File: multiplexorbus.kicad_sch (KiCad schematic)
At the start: 4 parts

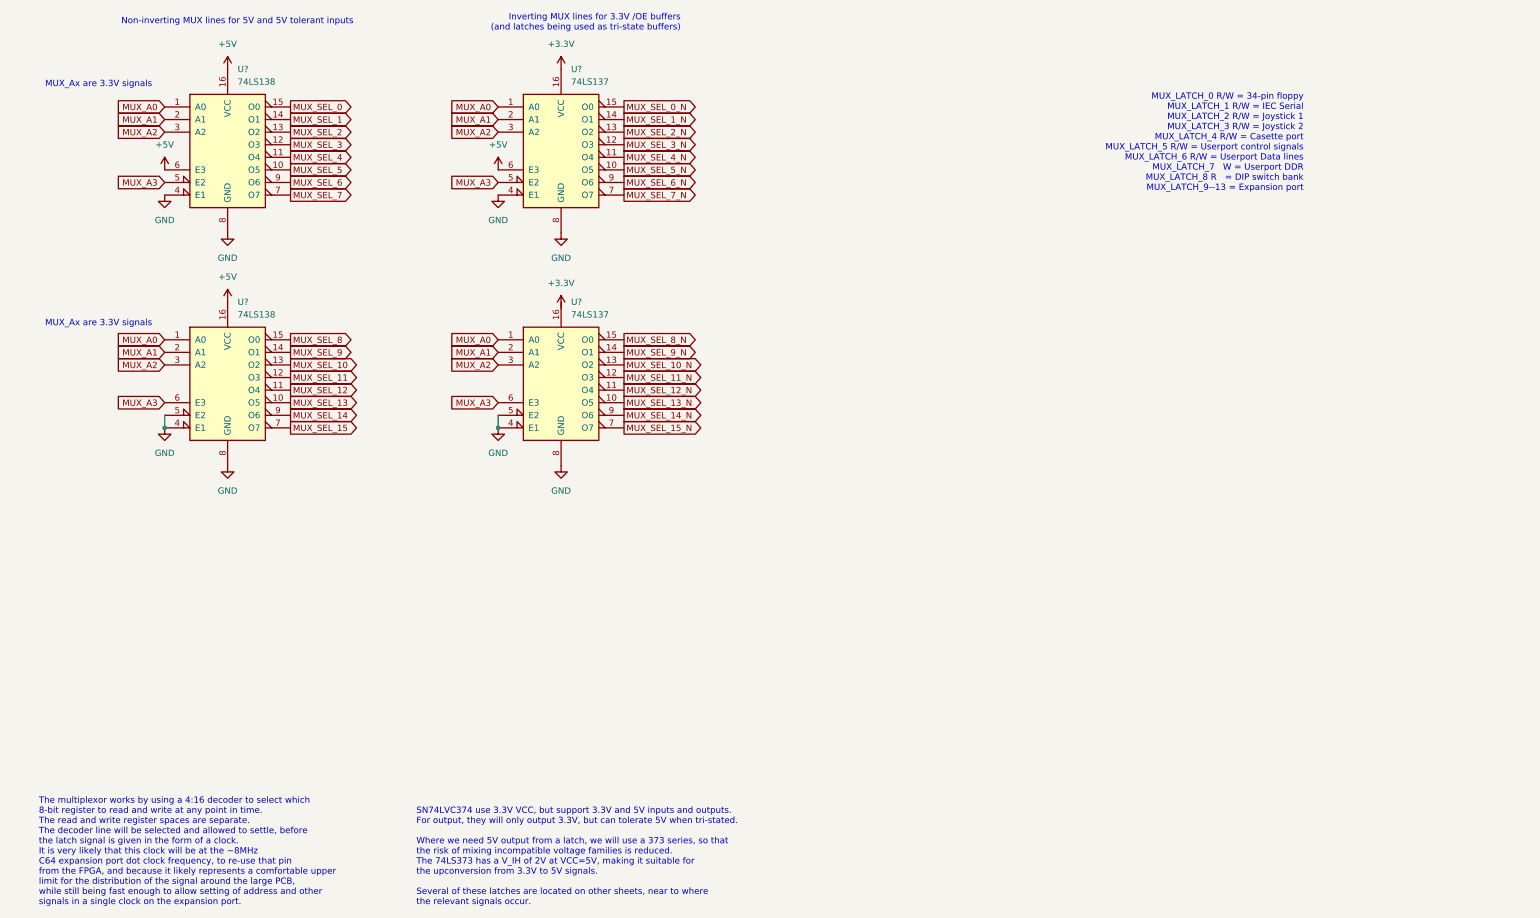
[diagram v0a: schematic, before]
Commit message: beautify the schematics, especially the title-page
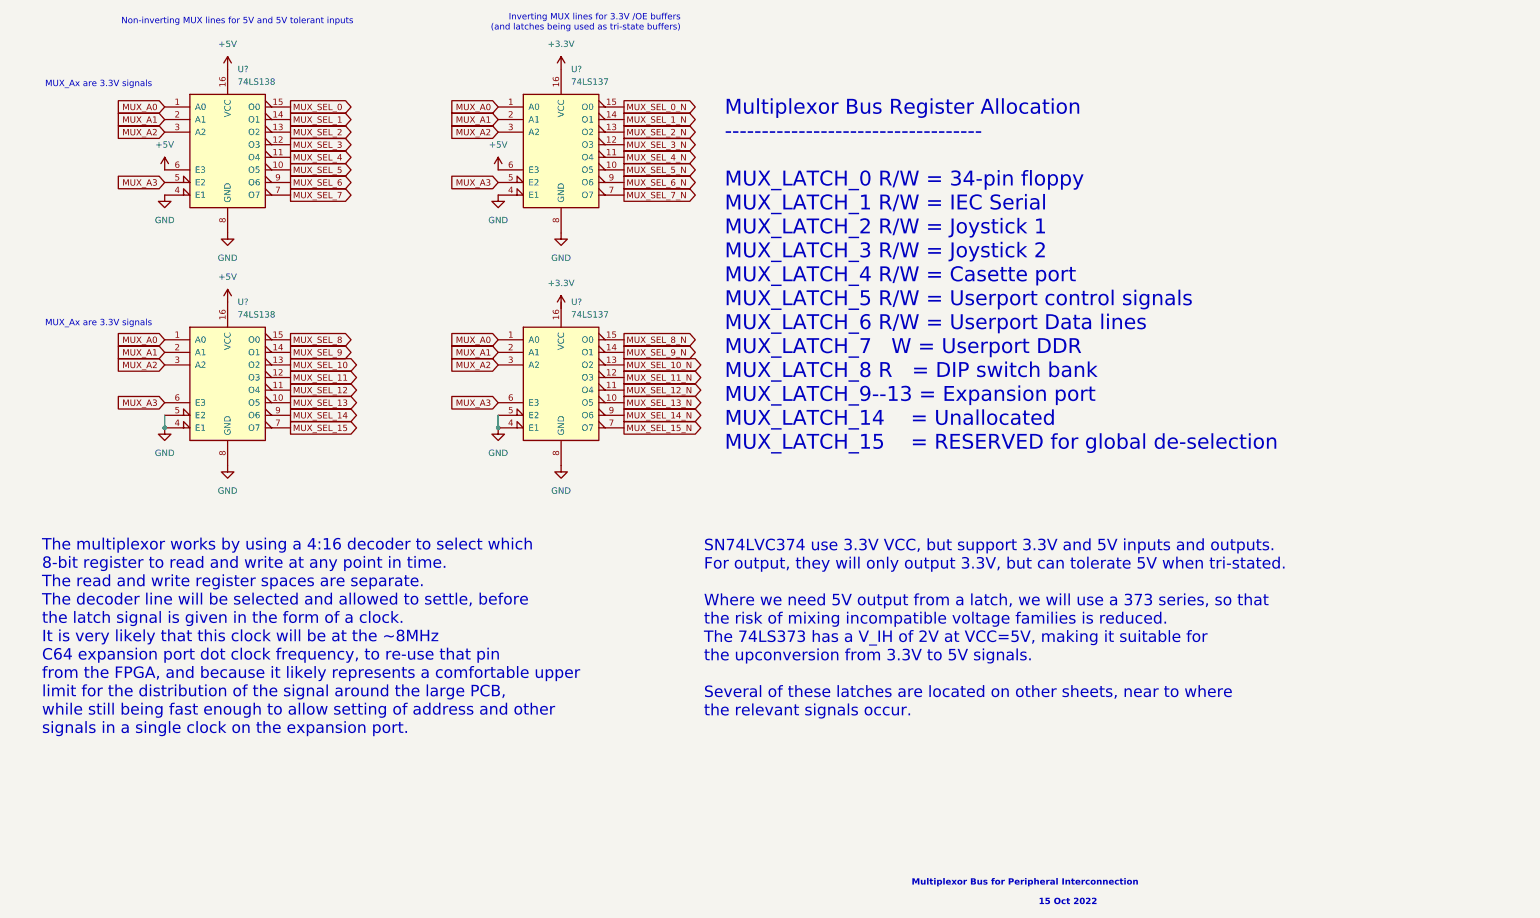
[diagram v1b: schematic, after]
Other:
- note added: "15 Oct 2022"
- note added: "Multiplexor Bus Register Allocation ----------------------------------- MUX_LATCH_0 R/W = 34-pin floppy MUX_LATCH_1 R/W = IEC Serial MUX_LATCH_2 R/W = Joystick 1 MUX_LATCH_3 R/W = Joystick 2 MUX_LATCH_4 R/W = Casette port MUX_LATCH_5 R/W = Userport control signals MUX_LATCH_6 R/W = Userport Data lines MUX_LATCH_7 W = Userport DDR MUX_LATCH_8 R = DIP switch bank MUX_LATCH_9--13 = Expansion port MU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"
- note added: "Multiplexor Bus for Peripheral Interconnection"
- note removed: "MUX_LATCH_0 R/W = 34-pin floppy MUX_LATCH_1 R/W = IEC Serial MUX_LATCH_2 R/W = Joystick 1 MUX_LATCH_3 R/W = Joystick 2 MUX_LATCH_4 R/W = Casette port MUX_LATCH_5 R/W = Userport control signals MUX_LATCH_6 R/W = Userport Data lines MUX_LATCH_7 W = Userport DDR MUX_LATCH_8 R = DIP switch bank MUX_LATCH_9--13 = Expansion port"

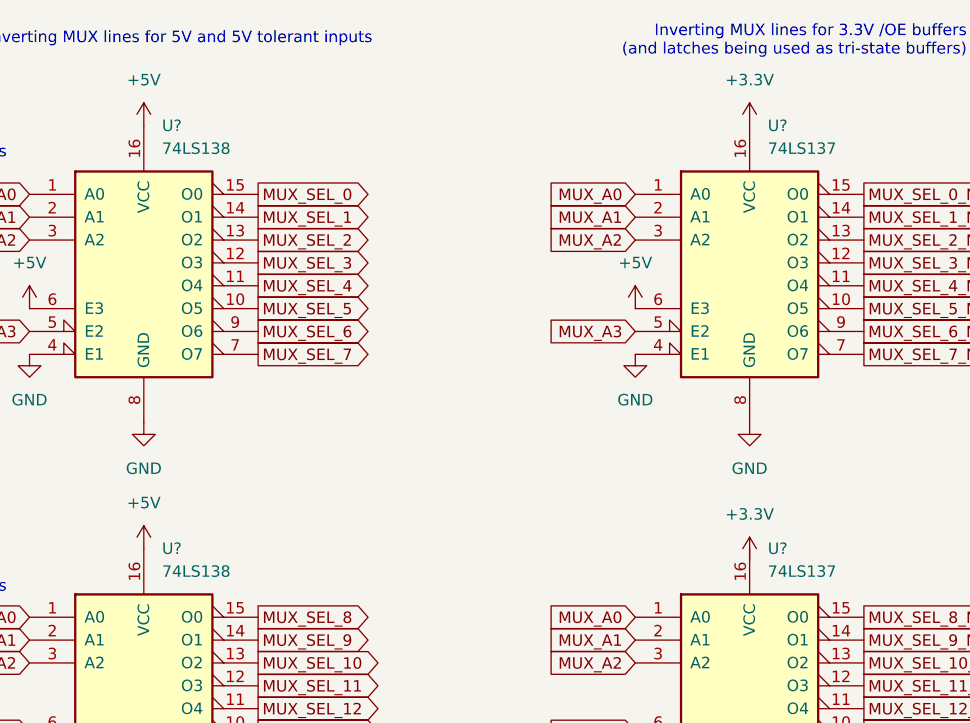
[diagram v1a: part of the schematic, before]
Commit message: add all missing footprints
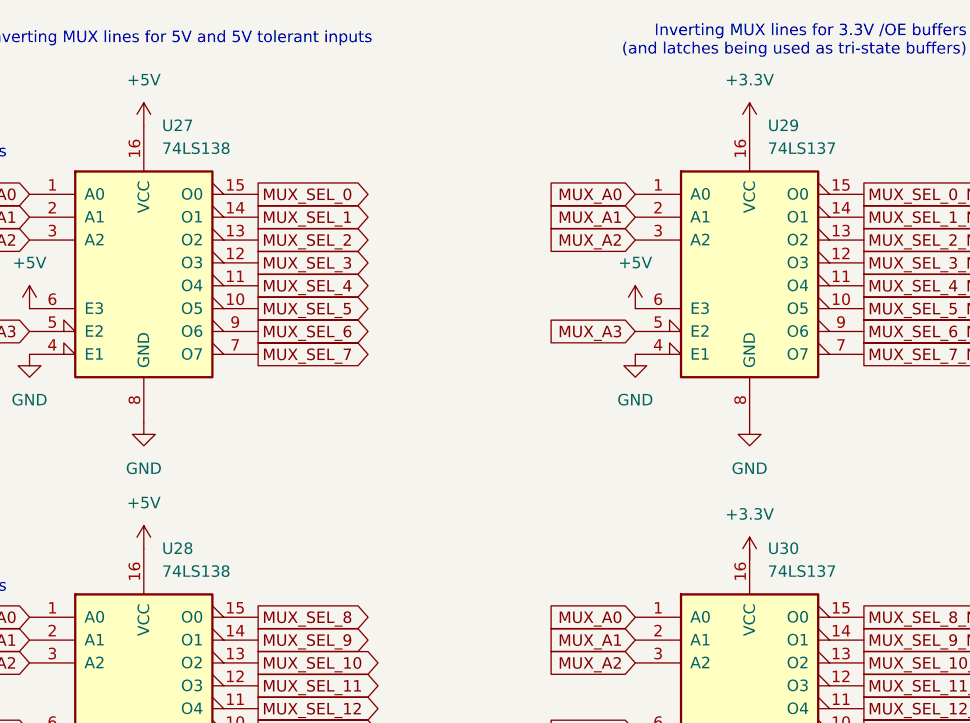
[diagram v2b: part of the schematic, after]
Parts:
- gave numbers to parts that had none: 4
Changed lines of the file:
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@@
   (symbol (lib_id "74xx:74LS138") (at 120.65 87.63 0) (unit 1)
     (in_bom yes) (on_board yes) (fields_autoplaced)
-    (property "Reference" "U?" (id 0) (at 122.6694 72.39 0)
+    (property "Reference" "U30" (id 0) (at 122.6694 72.39 0)
       (effects (font (size 1.27 1.27)) (justify left))
     )
@@
   (symbol (lib_id "74xx:74LS138") (at 120.65 40.64 0) (unit 1)
     (in_bom yes) (on_board yes) (fields_autoplaced)
-    (property "Reference" "U?" (id 0) (at 122.6694 25.4 0)
+    (property "Reference" "U29" (id 0) (at 122.6694 25.4 0)
       (effects (font (size 1.27 1.27)) (justify left))
     )
@@
   (symbol (lib_id "power:GND") (at 40.64 97.79 0) (unit 1)
     (in_bom yes) (on_board yes) (fields_autoplaced)
-    (property "Reference" "#PWR?" (id 0) (at 40.64 104.14 0)
+    (property "Reference" "#PWR0225" (id 0) (at 40.64 104.14 0)
       (effects (font (size 1.27 1.27)) hide)
     )
@@
   (symbol (lib_id "power:GND") (at 120.65 105.41 0) (unit 1)
     (in_bom yes) (on_board yes) (fields_autoplaced)
-    (property "Reference" "#PWR?" (id 0) (at 120.65 111.76 0)
+    (property "Reference" "#PWR0233" (id 0) (at 120.65 111.76 0)
       (effects (font (size 1.27 1.27)) hide)
     )
@@
   (symbol (lib_id "power:GND") (at 107.95 50.8 0) (unit 1)
     (in_bom yes) (on_board yes) (fields_autoplaced)
-    (property "Reference" "#PWR?" (id 0) (at 107.95 57.15 0)
+    (property "Reference" "#PWR0235" (id 0) (at 107.95 57.15 0)
       (effects (font (size 1.27 1.27)) hide)
     )
@@
   (symbol (lib_id "power:+3.3V") (at 120.65 25.4 0) (unit 1)
     (in_bom yes) (on_board yes) (fields_autoplaced)
-    (property "Reference" "#PWR?" (id 0) (at 120.65 29.21 0)
+    (property "Reference" "#PWR0231" (id 0) (at 120.65 29.21 0)
       (effects (font (size 1.27 1.27)) hide)
     )
@@
   (symbol (lib_id "power:GND") (at 53.34 58.42 0) (unit 1)
     (in_bom yes) (on_board yes) (fields_autoplaced)
-    (property "Reference" "#PWR?" (id 0) (at 53.34 64.77 0)
+    (property "Reference" "#PWR0230" (id 0) (at 53.34 64.77 0)
       (effects (font (size 1.27 1.27)) hide)
     )
@@
   (symbol (lib_id "power:+3.3V") (at 120.65 73.66 0) (unit 1)
     (in_bom yes) (on_board yes) (fields_autoplaced)
-    (property "Reference" "#PWR?" (id 0) (at 120.65 77.47 0)
+    (property "Reference" "#PWR0236" (id 0) (at 120.65 77.47 0)
       (effects (font (size 1.27 1.27)) hide)
     )
@@
   (symbol (lib_id "power:GND") (at 53.34 105.41 0) (unit 1)
     (in_bom yes) (on_board yes) (fields_autoplaced)
-    (property "Reference" "#PWR?" (id 0) (at 53.34 111.76 0)
+    (property "Reference" "#PWR0224" (id 0) (at 53.34 111.76 0)
       (effects (font (size 1.27 1.27)) hide)
     )
@@
   (symbol (lib_id "power:+5V") (at 53.34 25.4 0) (unit 1)
     (in_bom yes) (on_board yes) (fields_autoplaced)
-    (property "Reference" "#PWR?" (id 0) (at 53.34 29.21 0)
+    (property "Reference" "#PWR0227" (id 0) (at 53.34 29.21 0)
       (effects (font (size 1.27 1.27)) hide)
     )
@@
   (symbol (lib_id "power:GND") (at 120.65 58.42 0) (unit 1)
     (in_bom yes) (on_board yes) (fields_autoplaced)
-    (property "Reference" "#PWR?" (id 0) (at 120.65 64.77 0)
+    (property "Reference" "#PWR0237" (id 0) (at 120.65 64.77 0)
       (effects (font (size 1.27 1.27)) hide)
     )
@@
   (symbol (lib_id "74xx:74LS138") (at 53.34 87.63 0) (unit 1)
     (in_bom yes) (on_board yes) (fields_autoplaced)
-    (property "Reference" "U?" (id 0) (at 55.3594 72.39 0)
+    (property "Reference" "U28" (id 0) (at 55.3594 72.39 0)
       (effects (font (size 1.27 1.27)) (justify left))
     )
@@
   (symbol (lib_id "power:+5V") (at 107.95 45.72 0) (unit 1)
     (in_bom yes) (on_board yes) (fields_autoplaced)
-    (property "Reference" "#PWR?" (id 0) (at 107.95 49.53 0)
+    (property "Reference" "#PWR0232" (id 0) (at 107.95 49.53 0)
       (effects (font (size 1.27 1.27)) hide)
     )
@@
   (symbol (lib_id "power:GND") (at 107.95 97.79 0) (unit 1)
     (in_bom yes) (on_board yes) (fields_autoplaced)
-    (property "Reference" "#PWR?" (id 0) (at 107.95 104.14 0)
+    (property "Reference" "#PWR0234" (id 0) (at 107.95 104.14 0)
       (effects (font (size 1.27 1.27)) hide)
     )
@@
   (symbol (lib_id "power:+5V") (at 40.64 45.72 0) (unit 1)
     (in_bom yes) (on_board yes) (fields_autoplaced)
-    (property "Reference" "#PWR?" (id 0) (at 40.64 49.53 0)
+    (property "Reference" "#PWR0226" (id 0) (at 40.64 49.53 0)
       (effects (font (size 1.27 1.27)) hide)
     )
@@
   (symbol (lib_id "74xx:74LS138") (at 53.34 40.64 0) (unit 1)
     (in_bom yes) (on_board yes) (fields_autoplaced)
-    (property "Reference" "U?" (id 0) (at 55.3594 25.4 0)
+    (property "Reference" "U27" (id 0) (at 55.3594 25.4 0)
       (effects (font (size 1.27 1.27)) (justify left))
     )
@@
   (symbol (lib_id "power:GND") (at 40.64 50.8 0) (unit 1)
     (in_bom yes) (on_board yes) (fields_autoplaced)
-    (property "Reference" "#PWR?" (id 0) (at 40.64 57.15 0)
+    (property "Reference" "#PWR0229" (id 0) (at 40.64 57.15 0)
       (effects (font (size 1.27 1.27)) hide)
     )
@@
   (symbol (lib_id "power:+5V") (at 53.34 72.39 0) (unit 1)
     (in_bom yes) (on_board yes) (fields_autoplaced)
-    (property "Reference" "#PWR?" (id 0) (at 53.34 76.2 0)
-      (effects (font (size 1.27 1.27)) hide)
-    )
+    (property "Reference" "#PWR0228" (id 0) (at 53.34 76.2 0)
+      (effects (font (size 1.27 1.27)) hide)
+    )

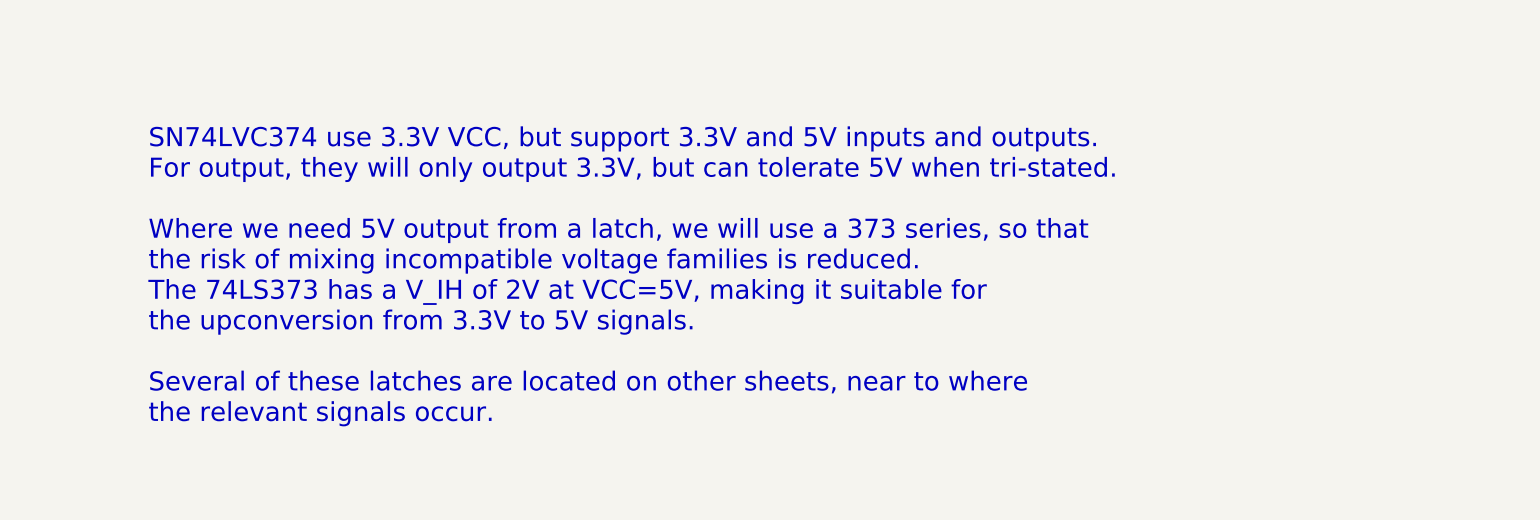
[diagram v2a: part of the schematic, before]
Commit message: replace 74LS373s with 74LS374s #5
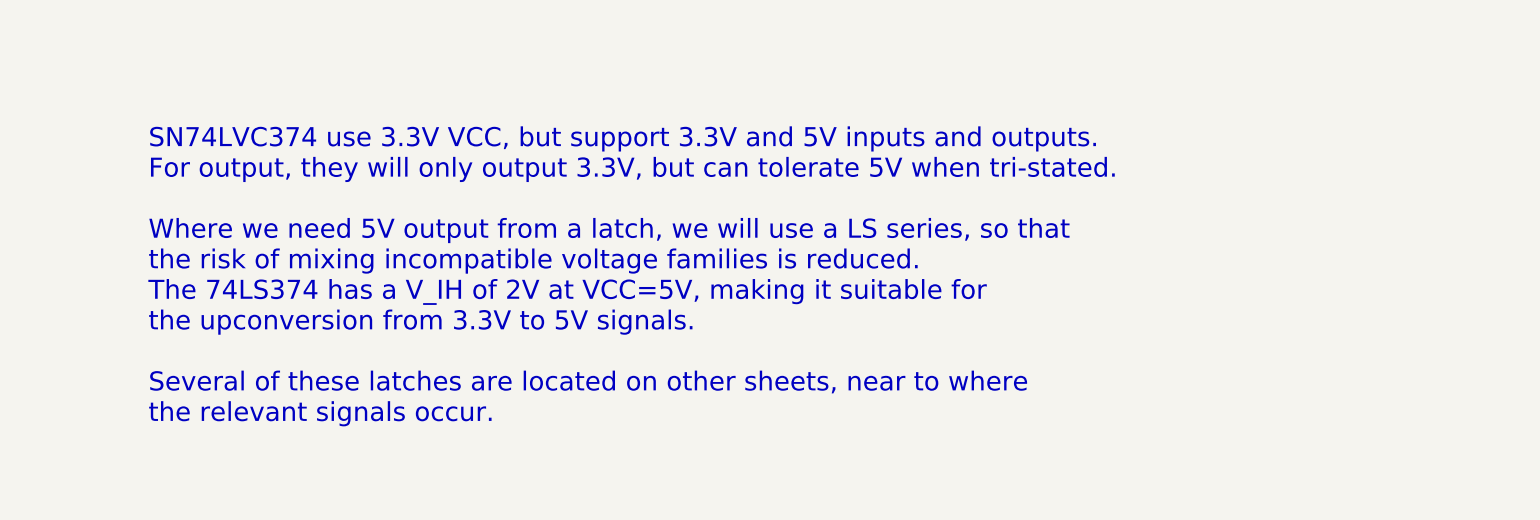
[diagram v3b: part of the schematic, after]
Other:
- note added: "SN74LVC374 use 3.3V VCC, but support 3.3V and 5V inputs and outputs. For output, they will only output 3.3V, but can tolerate 5V when tri-stated. Where we need 5V output from a latch, we will use a LS series, so that the risk of mixing incompatible voltage families is reduced. The 74LS374 has a V_IH of 2V at VCC=5V, making it suitable for the upconversion from 3.3V to 5V signals. Several of these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"
- note removed: "SN74LVC374 use 3.3V VCC, but support 3.3V and 5V inputs and outputs. For output, they will only output 3.3V, but can tolerate 5V when tri-stated. Where we need 5V output from a latch, we will use a 373 series, so that the risk of mixing incompatible voltage families is reduced. The 74LS373 has a V_IH of 2V at VCC=5V, making it suitable for the upconversion from 3.3V to 5V signals. Several of thes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"
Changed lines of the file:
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@@
     (effects (font (size 1.27 1.27)) (justify right bottom))
   )
-  (text "SN74LVC374 use 3.3V VCC, but support 3.3V and 5V inputs and outputs.\nFor output, they will only output 3.3V, but can tolerate 5V when tri-stated.\n\nWhere we need 5V output from a latch, we will use a 373 series, so that\nthe risk of mixing incompatible voltage families is reduced.\nThe 74LS373 has a V_IH of 2V at VCC=5V, making it suitable for\nthe upconversion from 3.3V to 5V signals.\n\nSeveral of these latches are located on other sheets, near to where\nthe relevant signals occur."
+  (text "SN74LVC374 use 3.3V VCC, but support 3.3V and 5V inputs and outputs.\nFor output, they will only output 3.3V, but can tolerate 5V when tri-stated.\n\nWhere we need 5V output from a latch, we will use a LS series, so that\nthe risk of mixing incompatible voltage families is reduced.\nThe 74LS374 has a V_IH of 2V at VCC=5V, making it suitable for\nthe upconversion from 3.3V to 5V signals.\n\nSeveral of these latches are located on other sheets, near to where\nthe relevant signals occur."
     (at 149.479 156.337 0)
     (effects (font (size 2.3 2.3)) (justify left bottom))
